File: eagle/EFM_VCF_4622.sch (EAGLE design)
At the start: 57 parts, among them IC1 LM13700N, Q1 2N3904, Q10 2N3904, Q11 2N3904, Q12 2N3904, Q13 2N3904, Q2 2N3904, Q3 2N3906, Q4 2N3904, Q5 2N3904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

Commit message: board progress
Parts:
- removed U$3: AUDIO-JACK, erthenvar:AUDIO-JACK
- added OUT: AUDIO-JACK, erthenvar:AUDIO-JACK
- renumbered U$1 to CV1, U$2 to IN1
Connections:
- removed net N$34: IN_2.MP
- net GND: now also OUT.RING; no longer U$3.RING
- net N$31: now also OUT.TIP; no longer U$3.TIP
- net N$5: now also IN_2.MP
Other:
- moved on the sheet: C1, C12, C2, C3, C6, IC1A, Q12, Q13, R10, R13, R2, R22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

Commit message: parts on the board
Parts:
- removed C12: 10uF, rcl:CPOL-USB45181A
- removed CV1: AUDIO-JACK, erthenvar:AUDIO-JACK
- removed CV1_LEVEL, IN1_LEVEL: 100k, pot:3RP/1610N
- removed R1: 4k7, rcl:R-US_0207/7
- removed R2: 100R, rcl:R-US_0207/7
- removed R23, R29: 10k, rcl:R-US_0207/7
- removed R5: 1k, rcl:R-US_0207/7
- removed RESONANCE: 10k, pot:3RP/1610N
- added C4: 0.1uF, rcl:C-US050-025X075
- added CV1_LEV, IN1_LEV: 100k, pot:3RP/1610N
- added CV_1: AUDIO-JACK, erthenvar:AUDIO-JACK
- added Q: 10k, pot:3RP/1610N
- added R21: 100R, rcl:R-US_0207/7
- added R24: 470k, rcl:R-US_0207/7
- added R25, R27: 10k, rcl:R-US_0207/7
- added R26: 33k, rcl:R-US_0207/7
- C5: value 10uF -> 0.1uF; device rcl:CPOL-USB45181A -> rcl:C-US050-025X075
- C6, C7: device rcl:C-US025-030X050 -> rcl:C-US050-025X075
- C8, C9: value 0.1uF -> 10uF; device rcl:C-US025-030X050 -> rcl:CPOL-USB45181A
- Q1: value 2N3904 -> 2N3906; device transistor-npn:2N3904 -> transistor-pnp:2N3906
- Q3: value 2N3906 -> 2N3904; device transistor-pnp:2N3906 -> transistor-npn:2N3904
- R10: value 100k -> 10k
- R11: value 150k -> 4k7
- R14: value 100R -> 1k
- R16: value 10k -> 1k
- R19: value 2k2 -> 1k
- R20: value 33k -> 2k2
- R22: value 470k -> 100R
- R3, R4, R8: value 1k -> 100k
- R6: value 100k -> 150k
- R9: value 100k -> 1k
- renumbered IN_2 to IN2, U1 to PWR1
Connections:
- removed net N$16: Q3.B, R11.1, R12.1, R6.1, R7.1
- new net N$20: Q1.B, R3.1, R4.1, R6.1, R9.1
- net +12V: now also Q13.C; no longer Q5.C
- net -12V: now also R25.2, R27.2, R6.2; no longer R1.2, R23.2, R29.2
- net GND: now also C8.-, C9.-, CV1_LEV.A, CV_1.RING, IN1_LEV.A, Q2.E, R24.2, R26.2, R9.2; no longer C10.-, C3.-, CV1.RING, CV1_LEVEL.A, IN1_LEVEL.A, Q4.E, R12.2, R19.2, R22.2
- net N$1: now also R24.1; no longer R22.1
- net N$10: now also C10.+, Q.E; no longer C11.+, RESONANCE.E
- net N$12: now also C4.1, Q8.E, Q9.C; no longer C6.1, Q11.C, Q13.E
- net N$13: now also C6.1, Q10.E, Q11.C; no longer C7.1, Q7.C, Q9.E
- net N$14: now also C5.2, Q4.E, Q5.C; no longer C8.2, Q10.E, Q8.C
- net N$15: now also C5.1, Q10.C, Q9.E; no longer C8.1, Q11.E, Q9.C
- net N$17: now also C7.1, Q11.E, Q12.C; no longer C9.1, Q2.C, Q7.E
- net N$18: now also C7.2, Q7.C; no longer C9.2, Q1.C
- net N$19: now also Q13.B, R26.1; no longer Q5.B, R20.1
- net N$2: now also Q.A, Q.S, R22.2; no longer R14.2, RESONANCE.A, RESONANCE.S
- net N$25: now also C8.+, R12.2, R17.2, R19.2, R20.1; no longer C10.+, R15.2, R18.2, R19.1, R3.2
- net N$26: now also Q12.B, R19.1, R22.1; no longer Q2.B, R14.1, R18.1
- net N$27: now also Q1.C, R11.1; no longer Q3.C, R1.1
- net N$28: now also C11.+, R27.1; no longer C12.+, R29.1
- net N$29: now also C6.2, Q5.E; no longer C7.2, Q8.E
- net N$3: now also Q2.C, R18.2; no longer Q4.C, R17.2
- net N$31: now also C11.-; no longer C12.-
- net N$35: now also C10.-, Q13.E, R25.1; no longer C11.-, Q5.E, R23.1
- net N$38: now also C9.+, R10.1, R21.2; no longer C3.+, R16.1, R2.2
- net N$4: now also Q12.E, Q7.E, R18.1; no longer Q1.E, Q2.E, R17.1
- net N$43: now also Q3.C, Q8.C, R21.1; no longer Q12.C, Q13.C, R2.1
- net N$44: now also Q3.B, Q8.B, R14.1; no longer Q12.B, Q13.B, R8.1
- net N$46: now also Q4.B, Q9.B, R14.2, R15.1; no longer Q10.B, Q11.B, R5.1, R8.2
- net N$49: now also Q10.B, Q5.B, R15.2, R16.1; no longer Q8.B, Q9.B, R4.1, R5.2
- net N$5: now also R7.2; no longer R10.2
- net N$50: now also Q11.B, R16.2, R17.1; no longer Q7.B, R3.1, R4.2
- net N$53: now also CV1_LEV.S, R4.2; no longer CV1_LEVEL.S, R7.2
- net N$55: now also CV_1.NORM; no longer CV1.NORM
- net N$56: now also R3.2; no longer R6.2
- net N$57: now also IN1_LEV.S, R8.1; no longer IN1_LEVEL.S, R9.1
- net N$58: now also IN1_LEV.E; no longer IN1_LEVEL.E
- net N$59: now also CV1_LEV.E, CV_1.TIP; no longer CV1.TIP, CV1_LEVEL.E
- net N$6: now also C3.-, R7.1, R8.2; no longer C5.-, R10.1, R9.2
- net N$7: now also C3.+, Q7.B, R12.1; no longer C5.+, Q1.B, R15.1
- net N$8: now also Q1.E, Q2.B, R10.2; no longer Q3.E, Q4.B, R16.2
- net N$9: now also C4.2, Q3.E, Q4.C; no longer C6.2, Q10.C, Q12.E
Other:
- moved on the sheet: C10, C11, C3, C6, C7, CUTOFF, IC1A, IN1, OUT, Q10, Q11, Q12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

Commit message: routed
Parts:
- C10, C3: device rcl:CPOL-USB45181A -> rcl:CPOL-USB45181B
- C11: device rcl:CPOL-USB45181A -> rcl:CPOL-USB45181C
- R10: device rcl:R-US_0207/7 -> rcl:R-US_0309/12
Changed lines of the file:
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@@
 <part name="P-3" library="supply1" deviceset="-12V" device=""/>
 <part name="Q2" library="transistor-npn" deviceset="2N3904" device=""/>
-<part name="C3" library="rcl" deviceset="CPOL-US" device="B45181A" value="10uF"/>
+<part name="C3" library="rcl" deviceset="CPOL-US" device="B45181B" value="10uF"/>
 <part name="R4" library="rcl" deviceset="R-US_" device="0207/7" value="100k"/>
 <part name="P+4" library="supply1" deviceset="+12V" device=""/>
@@
 <part name="R27" library="rcl" deviceset="R-US_" device="0207/7" value="10k"/>
 <part name="P-7" library="supply1" deviceset="-12V" device=""/>
-<part name="C11" library="rcl" deviceset="CPOL-US" device="B45181A" value="10uF"/>
+<part name="C11" library="rcl" deviceset="CPOL-US" device="B45181C" value="10uF"/>
 <part name="R18" library="rcl" deviceset="R-US_" device="0207/7" value="1k"/>
 <part name="GND7" library="supply1" deviceset="GND" device=""/>
-<part name="R10" library="rcl" deviceset="R-US_" device="0207/7" value="10k"/>
+<part name="R10" library="rcl" deviceset="R-US_" device="0309/12" value="10k"/>
 <part name="P+5" library="supply1" deviceset="+12V" device=""/>
 <part name="P-5" library="supply1" deviceset="-12V" device=""/>
 <part name="R12" library="rcl" deviceset="R-US_" device="0207/7" value="1k"/>
 <part name="R19" library="rcl" deviceset="R-US_" device="0207/7" value="1k"/>
-<part name="C10" library="rcl" deviceset="CPOL-US" device="B45181A" value="10uF"/>
+<part name="C10" library="rcl" deviceset="CPOL-US" device="B45181B" value="10uF"/>
 <part name="C8" library="rcl" deviceset="CPOL-US" device="B45181A" value="10uF"/>
 <part name="Q" library="pot" deviceset="3RP/1610N" device="" value="10k"/>

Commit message: fixed connections
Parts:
- R24: device rcl:R-US_0207/7 -> rcl:R-US_0309/12
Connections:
- removed net N$38: C1.+, C9.+, CUTOFF.E, PWR1.+12V, R10.1, R21.2
- net +12V: now also C1.+, C9.+, CUTOFF.E, PWR1.+12V, R10.1, R21.2

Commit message: will try cut
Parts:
- C11: device rcl:CPOL-USB45181C -> rcl:CPOL-USB45181B
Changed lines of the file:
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@@
 <part name="GND11" library="supply1" deviceset="GND" device=""/>
 <part name="R27" library="rcl" deviceset="R-US_" device="0207/7" value="10k"/>
-<part name="C11" library="rcl" deviceset="CPOL-US" device="B45181C" value="10uF"/>
+<part name="C11" library="rcl" deviceset="CPOL-US" device="B45181B" value="10uF"/>
 <part name="R18" library="rcl" deviceset="R-US_" device="0207/7" value="1k"/>
 <part name="GND7" library="supply1" deviceset="GND" device=""/>

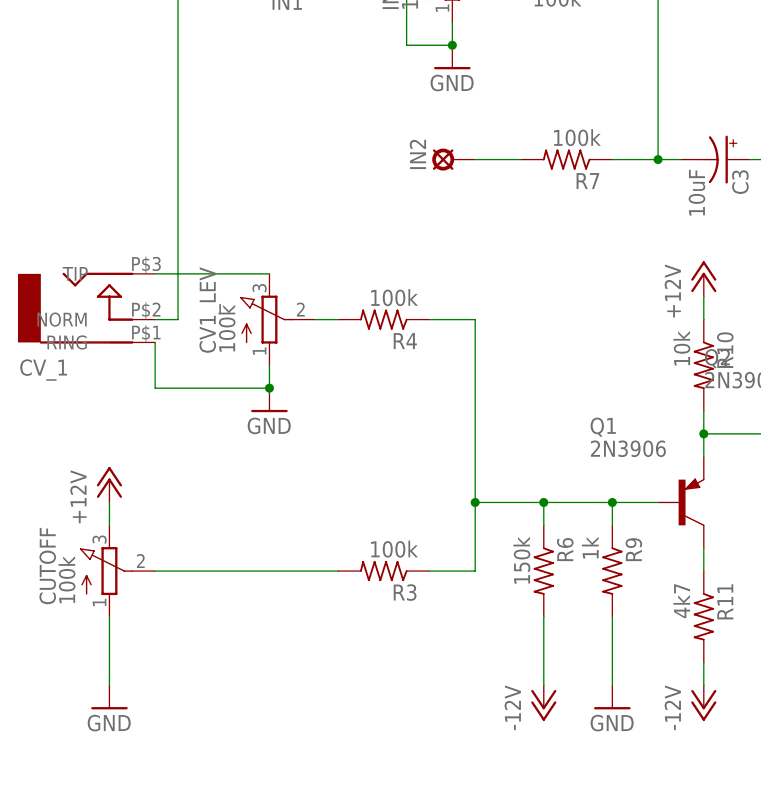
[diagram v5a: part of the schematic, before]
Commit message: neater layout and more cv and audio ins
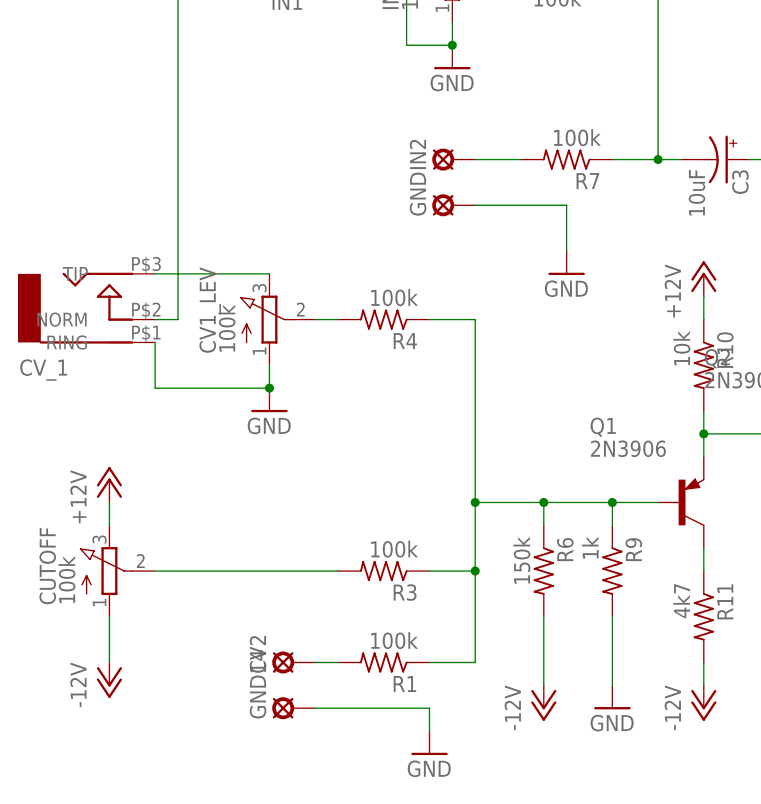
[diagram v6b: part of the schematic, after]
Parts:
- added CV2, GND, GND14: LSP10, solpad:LSP10
- added R1: 100k, rcl:R-US_0207/7
- C10: device rcl:CPOL-USB45181B -> rcl:CPOL-USB45181C
- C3: device rcl:CPOL-USB45181B -> rcl:CPOL-USB45181A
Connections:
- new net N$11: CV2.MP, R1.2
- net -12V: now also CUTOFF.A
- net GND: now also GND.MP, GND14.MP; no longer CUTOFF.A
- net N$20: now also R1.1
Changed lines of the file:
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@@
 <part name="R7" library="rcl" deviceset="R-US_" device="0207/7" value="100k"/>
 <part name="Q2" library="transistor-npn" deviceset="2N3904" device=""/>
-<part name="C3" library="rcl" deviceset="CPOL-US" device="B45181B" value="10uF"/>
+<part name="C3" library="rcl" deviceset="CPOL-US" device="B45181A" value="10uF"/>
 <part name="R4" library="rcl" deviceset="R-US_" device="0207/7" value="100k"/>
 <part name="CUTOFF" library="pot" deviceset="3RP/1610N" device="" value="100k"/>
 <part name="R3" library="rcl" deviceset="R-US_" device="0207/7" value="100k"/>
-<part name="GND2" library="supply1" deviceset="GND" device=""/>
 <part name="IN2" library="solpad" deviceset="LSP10" device=""/>
 <part name="IN1_LEV" library="pot" deviceset="3RP/1610N" device="" value="100k"/>
@@
 <part name="R12" library="rcl" deviceset="R-US_" device="0207/7" value="1k"/>
 <part name="R19" library="rcl" deviceset="R-US_" device="0207/7" value="1k"/>
-<part name="C10" library="rcl" deviceset="CPOL-US" device="B45181B" value="10uF"/>
+<part name="C10" library="rcl" deviceset="CPOL-US" device="B45181C" value="10uF"/>
 <part name="C8" library="rcl" deviceset="CPOL-US" device="B45181A" value="10uF"/>
 <part name="Q" library="pot" deviceset="3RP/1610N" device="" value="10k"/>
@@
 <part name="P-6" library="supply1" deviceset="-12V" device=""/>
 <part name="P-7" library="supply1" deviceset="-12V" device=""/>
+<part name="P-8" library="supply1" deviceset="-12V" device=""/>
+<part name="R1" library="rcl" deviceset="R-US_" device="0207/7" value="100k"/>
+<part name="CV2" library="solpad" deviceset="LSP10" device=""/>
+<part name="GND2" library="supply1" deviceset="GND" device=""/>
+<part name="GND" library="solpad" deviceset="LSP10" device=""/>
+<part name="GND14" library="solpad" deviceset="LSP10" device=""/>
+<part name="GND15" library="supply1" deviceset="GND" device=""/>
 </parts>
 <sheets>
@@
 <instance part="CUTOFF" gate="G$1" x="-99.06" y="15.24"/>
 <instance part="R3" gate="G$1" x="-68.58" y="15.24" rot="R180"/>
-<instance part="GND2" gate="1" x="-99.06" y="0"/>
 <instance part="IN2" gate="1" x="-60.96" y="60.96" rot="R90"/>
 <instance part="IN1_LEV" gate="G$1" x="-60.96" y="81.28"/>
@@
 <instance part="P-6" gate="1" x="-33.02" y="0"/>
 <instance part="P-7" gate="1" x="-50.8" y="0"/>
+<instance part="P-8" gate="1" x="-99.06" y="2.54"/>
+<instance part="R1" gate="G$1" x="-68.58" y="5.08" rot="R180"/>
+<instance part="CV2" gate="1" x="-78.74" y="5.08" rot="R90"/>
+<instance part="GND2" gate="1" x="-48.26" y="48.26"/>
+<instance part="GND" gate="1" x="-60.96" y="55.88" rot="R90"/>
+<instance part="GND14" gate="1" x="-78.74" y="0" rot="R90"/>
+<instance part="GND15" gate="1" x="-63.5" y="-5.08"/>
 </instances>
 <busses>
@@
 <pinref part="GND3" gate="1" pin="GND"/>
 <wire x1="-76.2" y1="119.38" x2="-63.5" y2="119.38" width="0.1524" layer="91"/>
-</segment>
-<segment>
-<pinref part="CUTOFF" gate="G$1" pin="A"/>
-<pinref part="GND2" gate="1" pin="GND"/>
-<wire x1="-99.06" y1="10.16" x2="-99.06" y2="2.54" width="0.1524" layer="91"/>
 </segment>
 <segment>
@@
 <pinref part="GND13" gate="1" pin="GND"/>
 <wire x1="93.98" y1="114.3" x2="93.98" y2="119.38" width="0.1524" layer="91"/>
+</segment>
+<segment>
+<pinref part="GND2" gate="1" pin="GND"/>
+<wire x1="-48.26" y1="50.8" x2="-48.26" y2="55.88" width="0.1524" layer="91"/>
+<pinref part="GND" gate="1" pin="MP"/>
+<wire x1="-48.26" y1="55.88" x2="-58.42" y2="55.88" width="0.1524" layer="91"/>
+</segment>
+<segment>
+<pinref part="GND15" gate="1" pin="GND"/>
+<wire x1="-63.5" y1="-2.54" x2="-63.5" y2="0" width="0.1524" layer="91"/>
+<pinref part="GND14" gate="1" pin="MP"/>
+<wire x1="-63.5" y1="0" x2="-76.2" y2="0" width="0.1524" layer="91"/>
 </segment>
 </net>
@@
 <wire x1="-58.42" y1="15.24" x2="-58.42" y2="22.86" width="0.1524" layer="91"/>
 <junction x="-58.42" y="22.86"/>
+<pinref part="R1" gate="G$1" pin="1"/>
+<wire x1="-63.5" y1="5.08" x2="-58.42" y2="5.08" width="0.1524" layer="91"/>
+<wire x1="-58.42" y1="5.08" x2="-58.42" y2="15.24" width="0.1524" layer="91"/>
+<junction x="-58.42" y="15.24"/>
 </segment>
 </net>
@@
 <pinref part="P-2" gate="1" pin="-12V"/>
 </segment>
-</net>
+<segment>
+<pinref part="CUTOFF" gate="G$1" pin="A"/>
+<wire x1="-99.06" y1="10.16" x2="-99.06" y2="5.08" width="0.1524" layer="91"/>
+<pinref part="P-8" gate="1" pin="-12V"/>
+</segment>
+</net>
+<net name="N$11" class="0">
+<segment>
+<pinref part="R1" gate="G$1" pin="2"/>
+<pinref part="CV2" gate="1" pin="MP"/>
+<wire x1="-76.2" y1="5.08" x2="-73.66" y2="5.08" width="0.1524" layer="91"/>
+</segment>
+</net>

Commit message: tidied still more
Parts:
- R10: device rcl:R-US_0309/12 -> rcl:R-US_0309/10
- R24: device rcl:R-US_0309/12 -> rcl:R-US_0207/7
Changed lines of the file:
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@@
 <part name="C6" library="rcl" deviceset="C-US" device="050-025X075" value="0.1uF"/>
 <part name="C4" library="rcl" deviceset="C-US" device="050-025X075" value="0.1uF"/>
-<part name="R24" library="rcl" deviceset="R-US_" device="0309/12" value="470k"/>
+<part name="R24" library="rcl" deviceset="R-US_" device="0207/7" value="470k"/>
 <part name="GND11" library="supply1" deviceset="GND" device=""/>
 <part name="R27" library="rcl" deviceset="R-US_" device="0207/7" value="10k"/>
@@
 <part name="R18" library="rcl" deviceset="R-US_" device="0207/7" value="1k"/>
 <part name="GND7" library="supply1" deviceset="GND" device=""/>
-<part name="R10" library="rcl" deviceset="R-US_" device="0309/12" value="10k"/>
+<part name="R10" library="rcl" deviceset="R-US_" device="0309/10" value="10k"/>
 <part name="R12" library="rcl" deviceset="R-US_" device="0207/7" value="1k"/>
 <part name="R19" library="rcl" deviceset="R-US_" device="0207/7" value="1k"/>
